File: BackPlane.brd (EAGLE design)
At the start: 134.6 x 116.5 mm, 16 parts

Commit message: More Routing
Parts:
- added U$10, U$5, U$6: T2I, BackplaneParts:T2I
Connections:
- net +5V: now also U$5.2, U$5.3, U$5.4
- net +5V_GND: now also U$6.2, U$6.3, U$6.4
- net CAN_H: now also U$10.2
- net CAN_L: now also U$10.3
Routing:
- net CAN_L: track 0.00 -> 19.6 mm
- net CAN_H: track 0.00 -> 16.5 mm
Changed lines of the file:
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@@
 <setting verticaltext="up"/>
 </settings>
-<grid distance="0.5" unitdist="mm" unit="mm" style="lines" multiple="1" display="yes" altdistance="0.05" altunitdist="mil" altunit="mil"/>
+<grid distance="0.1" unitdist="mm" unit="mm" style="lines" multiple="1" display="yes" altdistance="0.05" altunitdist="mil" altunit="mil"/>
 <layers>
 <layer number="1" name="Top" color="4" fill="1" visible="yes" active="yes"/>
@@
 <element name="ESC5_CON11" library="afro_20A_esc" package="3PINCONNECTOR" value="3PINCONNECTOR" x="112.17545625" y="82.261340625" rot="MR120"/>
 <element name="ESC5_CON12" library="afro_20A_esc" package="3PINCONNECTOR" value="3PINCONNECTOR" x="103.3983875" y="67.127509375" rot="MR120"/>
+<element name="U$10" library="BackplaneParts" package="T2I" value="T2I" x="57.7" y="115.2" rot="MR180"/>
+<element name="U$5" library="BackplaneParts" package="T2I" value="T2I" x="66.1" y="83.5" rot="MR90"/>
+<element name="U$6" library="BackplaneParts" package="T2I" value="T2I" x="74.2" y="83.5" rot="MR90"/>
 </elements>
 <signals>
@@
 <contactref element="U$3" pad="23"/>
 <contactref element="U$4" pad="23"/>
-<wire x1="106.411753125" y1="50.131184375" x2="61.45" y2="107.79" width="0" layer="19" extent="1-1"/>
-<wire x1="34.00970625" y1="40.008084375" x2="106.411753125" y2="50.131184375" width="0" layer="19" extent="1-1"/>
+<contactref element="U$10" pad="3"/>
+<wire x1="61.45" y1="107.79" x2="61.45" y2="109.25" width="0.254" layer="1"/>
+<wire x1="62.5" y1="110.3" x2="68.7" y2="110.3" width="0.254" layer="1"/>
+<wire x1="68.7" y1="110.3" x2="69.8" y2="111.4" width="0.254" layer="1"/>
+<wire x1="69.8" y1="111.4" x2="69.8" y2="112.4" width="0.254" layer="1"/>
+<wire x1="61.45" y1="109.25" x2="62.5" y2="110.3" width="0.254" layer="1"/>
+<wire x1="61.45" y1="107.79" x2="61.45" y2="106.95" width="0.254" layer="16"/>
+<wire x1="61.2" y1="106.7" x2="57.4" y2="106.7" width="0.254" layer="16"/>
+<wire x1="57.4" y1="106.7" x2="57.1" y2="106.4" width="0.254" layer="16"/>
+<wire x1="57.1" y1="106.4" x2="57.1" y2="103.9" width="0.254" layer="16"/>
+<wire x1="61.45" y1="106.95" x2="61.2" y2="106.7" width="0.254" layer="16"/>
+<wire x1="34.00970625" y1="40.008084375" x2="57.1" y2="103.9" width="0" layer="19" extent="16-16"/>
+<wire x1="106.411753125" y1="50.131184375" x2="68.7" y2="110.3" width="0" layer="19" extent="1-1"/>
 </signal>
 <signal name="CAN_H">
@@
 <contactref element="U$3" pad="24"/>
 <contactref element="U$4" pad="24"/>
-<wire x1="107.681753125" y1="52.3308875" x2="58.91" y2="107.79" width="0" layer="19" extent="1-1"/>
-<wire x1="35.27970625" y1="37.80838125" x2="107.681753125" y2="52.3308875" width="0" layer="19" extent="1-1"/>
+<contactref element="U$10" pad="2"/>
+<wire x1="58.91" y1="107.79" x2="62.22" y2="111.1" width="0.254" layer="1"/>
+<wire x1="62.22" y1="111.1" x2="66.8" y2="111.1" width="0.254" layer="1"/>
+<wire x1="66.8" y1="111.1" x2="67.8" y2="112.1" width="0.254" layer="1"/>
+<wire x1="67.8" y1="112.1" x2="67.8" y2="112.4" width="0.254" layer="1"/>
+<wire x1="58.91" y1="107.79" x2="57.89" y2="107.79" width="0.254" layer="16"/>
+<wire x1="57.89" y1="107.79" x2="56.5" y2="106.4" width="0.254" layer="16"/>
+<wire x1="56.5" y1="106.4" x2="56.5" y2="103.9" width="0.254" layer="16"/>
+<wire x1="66.8" y1="111.1" x2="107.681753125" y2="52.3308875" width="0" layer="19" extent="1-1"/>
+<wire x1="35.27970625" y1="37.80838125" x2="56.5" y2="103.9" width="0" layer="19" extent="16-16"/>
 </signal>
 <signal name="+12V">
@@
 <contactref element="U$4" pad="8"/>
 <polygon width="0.1524" layer="1">
-<vertex x="57.6" y="106.5"/>
+<vertex x="57.6" y="106.4"/>
 <vertex x="57.6" y="101.4"/>
 <vertex x="62.6" y="101.4"/>
-<vertex x="62.6" y="106.5"/>
+<vertex x="62.6" y="106.4"/>
 </polygon>
 <polygon width="0.1524" layer="1">
@@
 <vertex x="99.874165625" y="46.24929375"/>
 </polygon>
-<wire x1="32.3994125" y1="47.8772" x2="99.132046875" y2="42.602365625" width="0" layer="19" extent="1-1"/>
-<wire x1="71.61" y1="105.25" x2="100.402046875" y2="44.80206875" width="0" layer="19" extent="1-1"/>
+<contactref element="U$5" pad="4"/>
+<contactref element="U$5" pad="3"/>
+<contactref element="U$5" pad="2"/>
+<polygon width="0.1524" layer="1">
+<vertex x="72.8" y="104.3"/>
+<vertex x="72.8" y="93.9"/>
+<vertex x="71.2" y="92.3"/>
+<vertex x="68.5" y="92.3"/>
+<vertex x="67.9" y="92.9"/>
+<vertex x="67.9" y="101.6"/>
+<vertex x="68.1" y="101.8"/>
+<vertex x="68.1" y="104.1"/>
+<vertex x="72.6" y="104.1"/>
+</polygon>
+<wire x1="68.9" y1="93.6" x2="100.402046875" y2="44.80206875" width="0" layer="19" extent="1-1"/>
+<wire x1="31.1294125" y1="50.076903125" x2="68.9" y2="93.6" width="0" layer="19" extent="1-1"/>
 </signal>
 <signal name="+5V_GND">
@@
 <vertex x="99.217690625" y="35.312246875"/>
 </polygon>
-<wire x1="29.8594125" y1="52.276609375" x2="96.592046875" y2="38.20295625" width="0" layer="19" extent="1-1"/>
-<wire x1="76.69" y1="105.25" x2="97.862046875" y2="40.402659375" width="0" layer="19" extent="1-1"/>
+<polygon width="0.1524" layer="1">
+<vertex x="73.2" y="104.1"/>
+<vertex x="73.2" y="93.9"/>
+<vertex x="74.7" y="92.4"/>
+<vertex x="78.1" y="92.4"/>
+<vertex x="78.9" y="93.2"/>
+<vertex x="78.9" y="100.9"/>
+<vertex x="77.9" y="101.9"/>
+<vertex x="77.9" y="104.1"/>
+</polygon>
+<contactref element="U$6" pad="4"/>
+<contactref element="U$6" pad="3"/>
+<contactref element="U$6" pad="2"/>
+<wire x1="77" y1="93.6" x2="97.862046875" y2="40.402659375" width="0" layer="19" extent="1-1"/>
+<wire x1="28.5894125" y1="54.4763125" x2="77" y2="93.6" width="0" layer="19" extent="1-1"/>
 </signal>
 <signal name="R5">

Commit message: Routed
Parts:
- added U$11, U$12, U$15, U$16, U$7, U$8, U$9: T2I, BackplaneParts:T2I
- moved U$6 20.4 mm to (79.5, 63.8)
- moved U$5 13.8 mm to (71.8, 71.0)
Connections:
- net +12V: now also U$15.2, U$15.3, U$15.4, U$7.2, U$7.3, U$7.4, U$9.2, U$9.3, U$9.4
- net +12V_GND: now also U$11.2, U$11.3, U$11.4, U$16.2, U$16.3, U$16.4, U$2.5, U$2.6, U$3.5, U$3.6, U$4.5, U$4.6, U$8.2, U$8.3, U$8.4; no longer U$2.21, U$2.22, U$3.21, U$3.22, U$4.21, U$4.22
- net +5V: now also U$2.3, U$2.4, U$3.3, U$3.4, U$4.3, U$4.4; no longer U$2.19, U$2.20, U$3.19, U$3.20, U$4.19, U$4.20
- net +5V_GND: now also U$2.1, U$2.2, U$3.1, U$3.2, U$4.1, U$4.2; no longer U$2.17, U$2.18, U$3.17, U$3.18, U$4.17, U$4.18
- net CAN_H: now also U$12.2
- net CAN_L: now also U$12.3
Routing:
- net CAN_H: track 16.5 -> 299.8 mm
- net CAN_L: track 19.6 -> 285.8 mm
- net +5V_GND: track 0.00 -> 107.1 mm, vias 0 -> 1
- net +5V: track 0.00 -> 99.0 mm
- net +12V_GND: track 0.00 -> 77.6 mm
- net +12V: track 0.00 -> 76.8 mm
- net R3: track 5.86 -> 7.99 mm
- net R2: track 6.06 -> 8.07 mm
- net B4: track 5.92 -> 7.92 mm
- net Y8: track 6.05 -> 8.02 mm
- net B8: track 5.99 -> 7.79 mm
- net B5: track 6.45 -> 8.15 mm
- net R12: track 6.04 -> 7.68 mm
- net Y12: track 6.07 -> 7.65 mm
- added copper zone on layer 16, net +12V_GND
- added copper zone on layer 16, net +5V
- added copper zone on layer 16, net +5V_GND

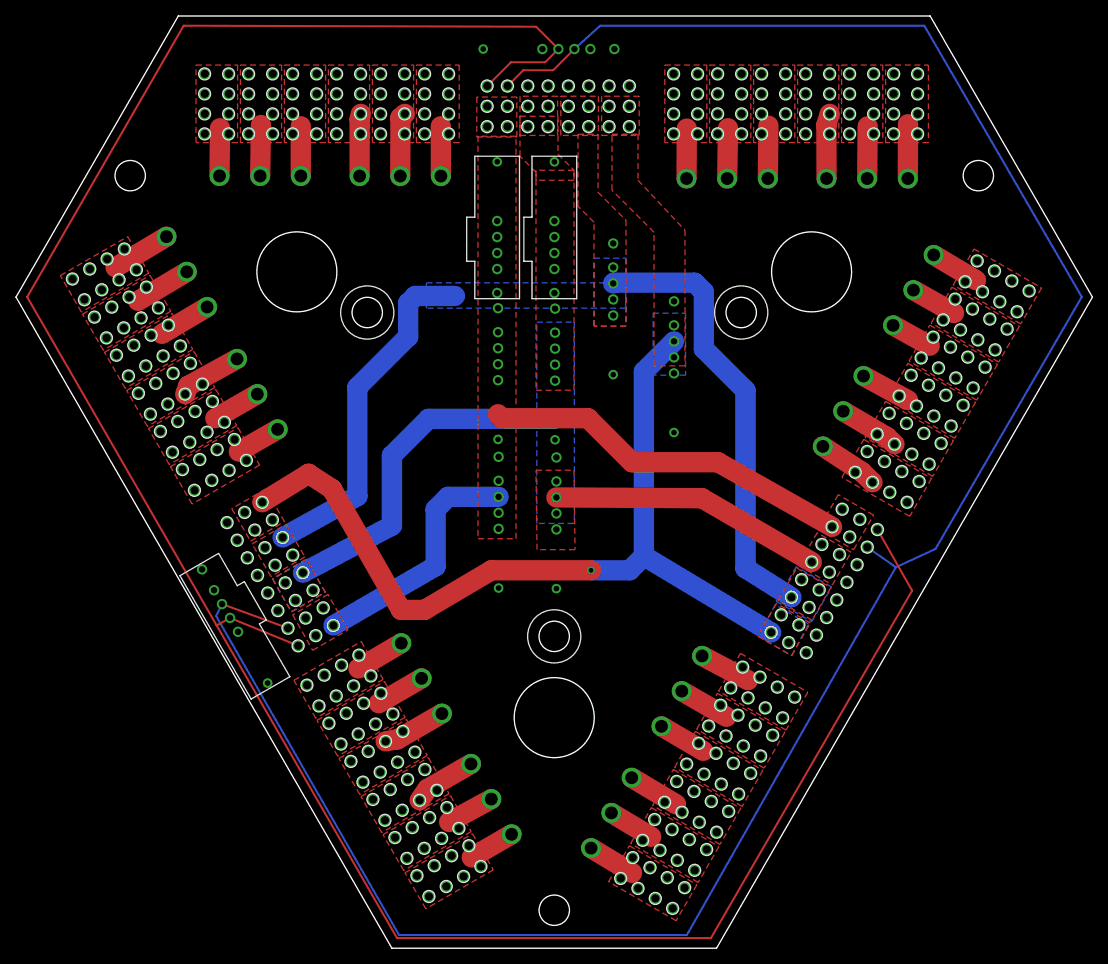
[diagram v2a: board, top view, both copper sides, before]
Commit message: Fixed clearance issues between the polygons by making them alternate layers
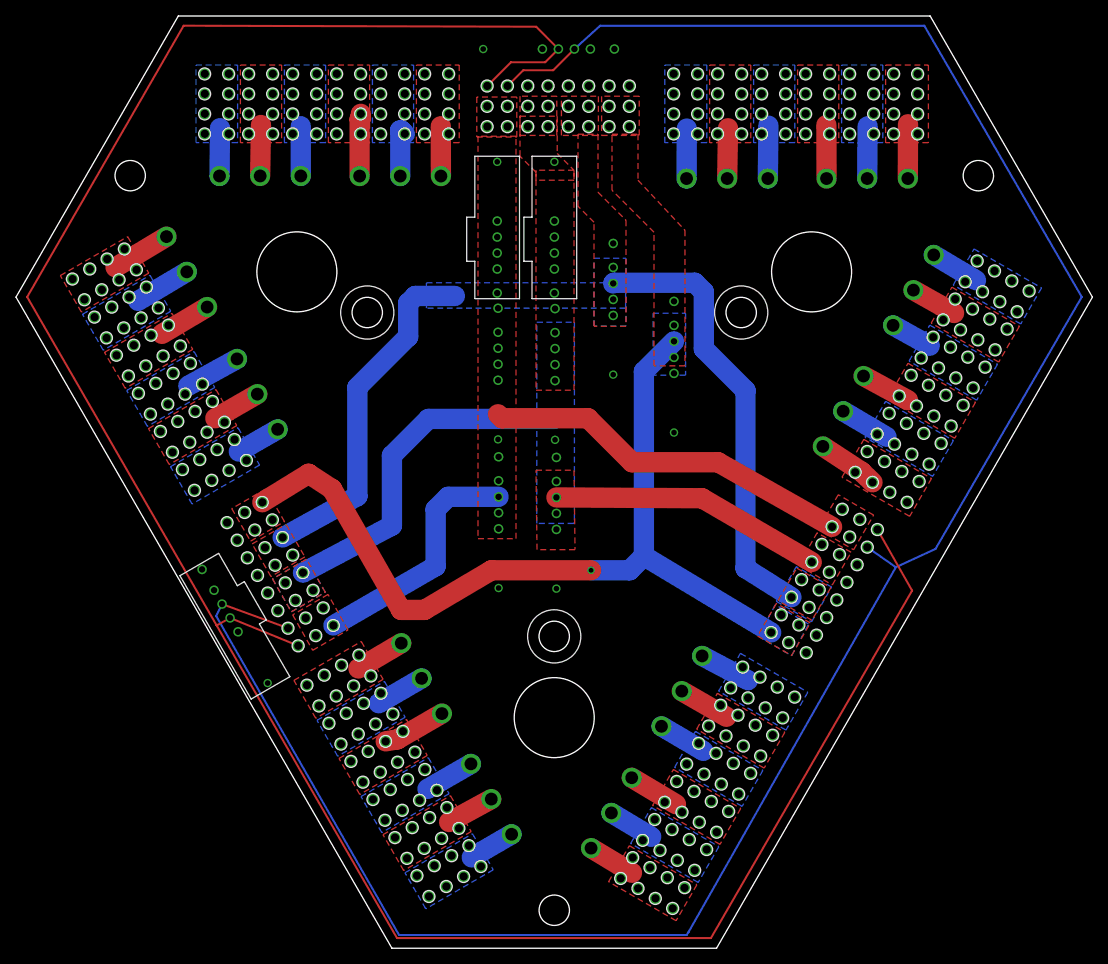
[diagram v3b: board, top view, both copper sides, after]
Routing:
- net R3: track 7.99 -> 6.27 mm
- net Y8: track 8.02 -> 6.46 mm
- net B5: track 8.15 -> 6.68 mm
- net Y12: track 7.65 -> 6.29 mm
- net R2: track 8.07 -> 6.95 mm
- added copper zone on layer 16, net B10
- added copper zone on layer 16, net B11
- added copper zone on layer 16, net B2
- added copper zone on layer 16, net B3
- added copper zone on layer 16, net B6
- added copper zone on layer 16, net B7
- added copper zone on layer 16, net R10
- added copper zone on layer 16, net R11
- added copper zone on layer 16, net R2
- added copper zone on layer 16, net R3
- added copper zone on layer 16, net R6
- added copper zone on layer 16, net R7
- added copper zone on layer 16, net Y1
- added copper zone on layer 16, net Y12
- added copper zone on layer 16, net Y4
- added copper zone on layer 16, net Y5
- added copper zone on layer 16, net Y8
- added copper zone on layer 16, net Y9
- removed copper zone on layer 1, net B10
- removed copper zone on layer 1, net B11
- removed copper zone on layer 1, net B2
- removed copper zone on layer 1, net B3
- removed copper zone on layer 1, net B6
- removed copper zone on layer 1, net B7
- removed copper zone on layer 1, net R10
- removed copper zone on layer 1, net R11
- removed copper zone on layer 1, net R2
- removed copper zone on layer 1, net R3
- removed copper zone on layer 1, net R6
- removed copper zone on layer 1, net R7
- removed copper zone on layer 1, net Y1
- removed copper zone on layer 1, net Y12
- removed copper zone on layer 1, net Y4
- removed copper zone on layer 1, net Y5
- removed copper zone on layer 1, net Y8
- removed copper zone on layer 1, net Y9
